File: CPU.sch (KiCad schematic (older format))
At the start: 14 parts, among them J8 SWD, U4 STM32F405RGTx, Y1 8MHz

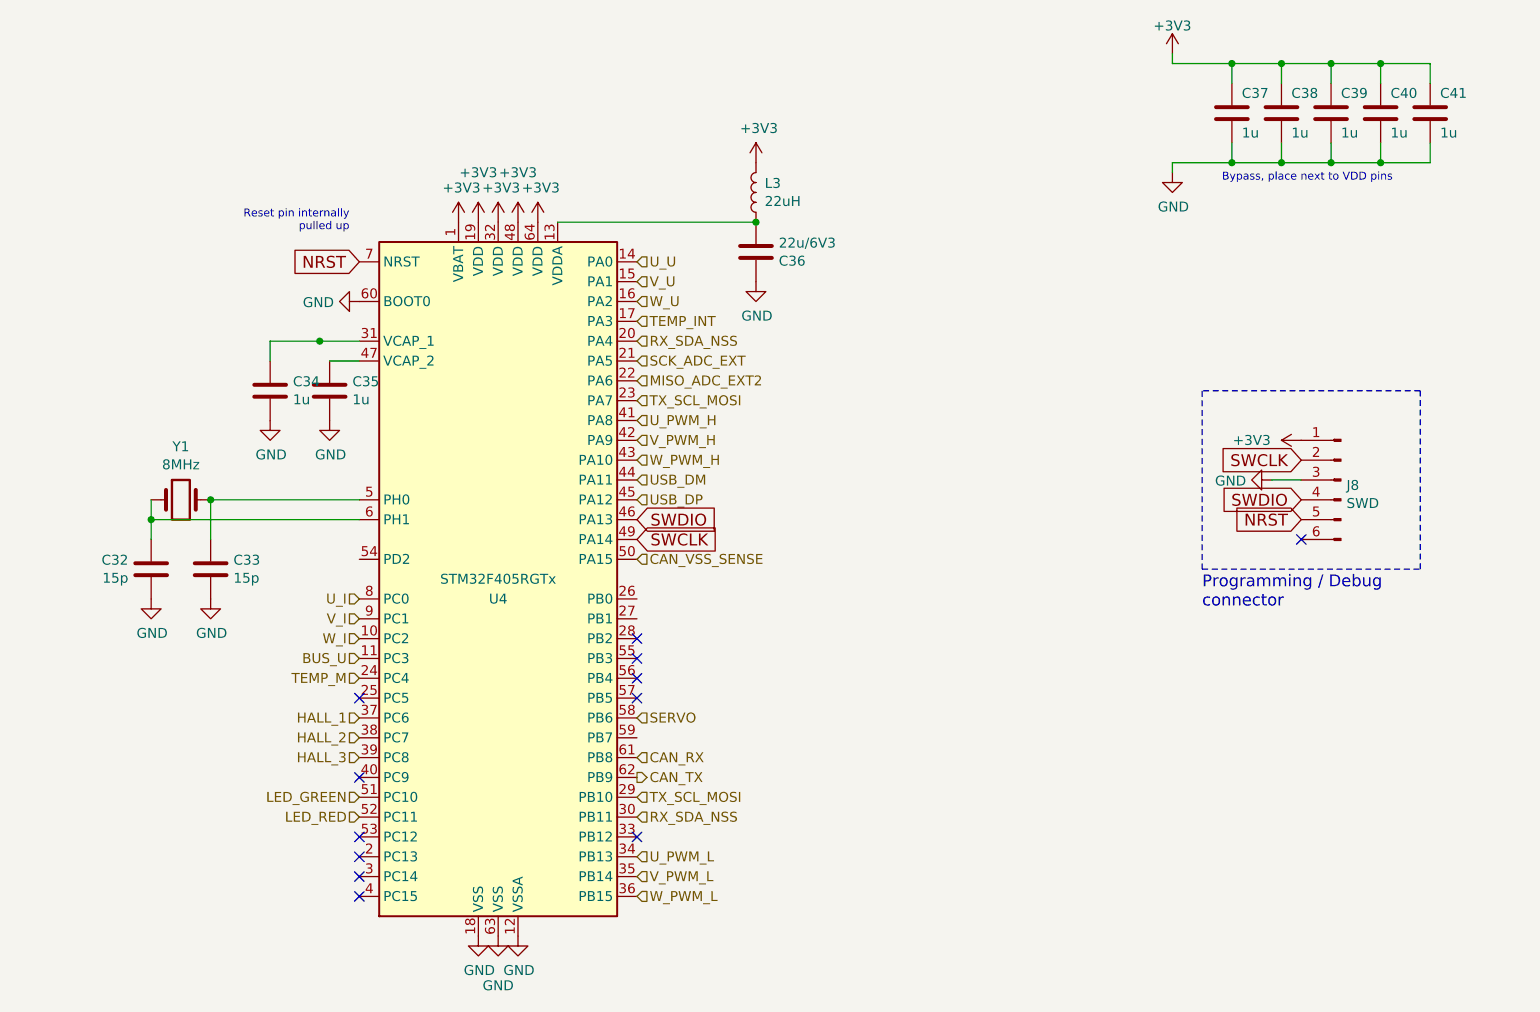
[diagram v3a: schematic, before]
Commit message: - reworked IO section -> now fully isolated - added fan output - sensor IO is now differential - exposed differential UART interface - fan pin not defined yet!
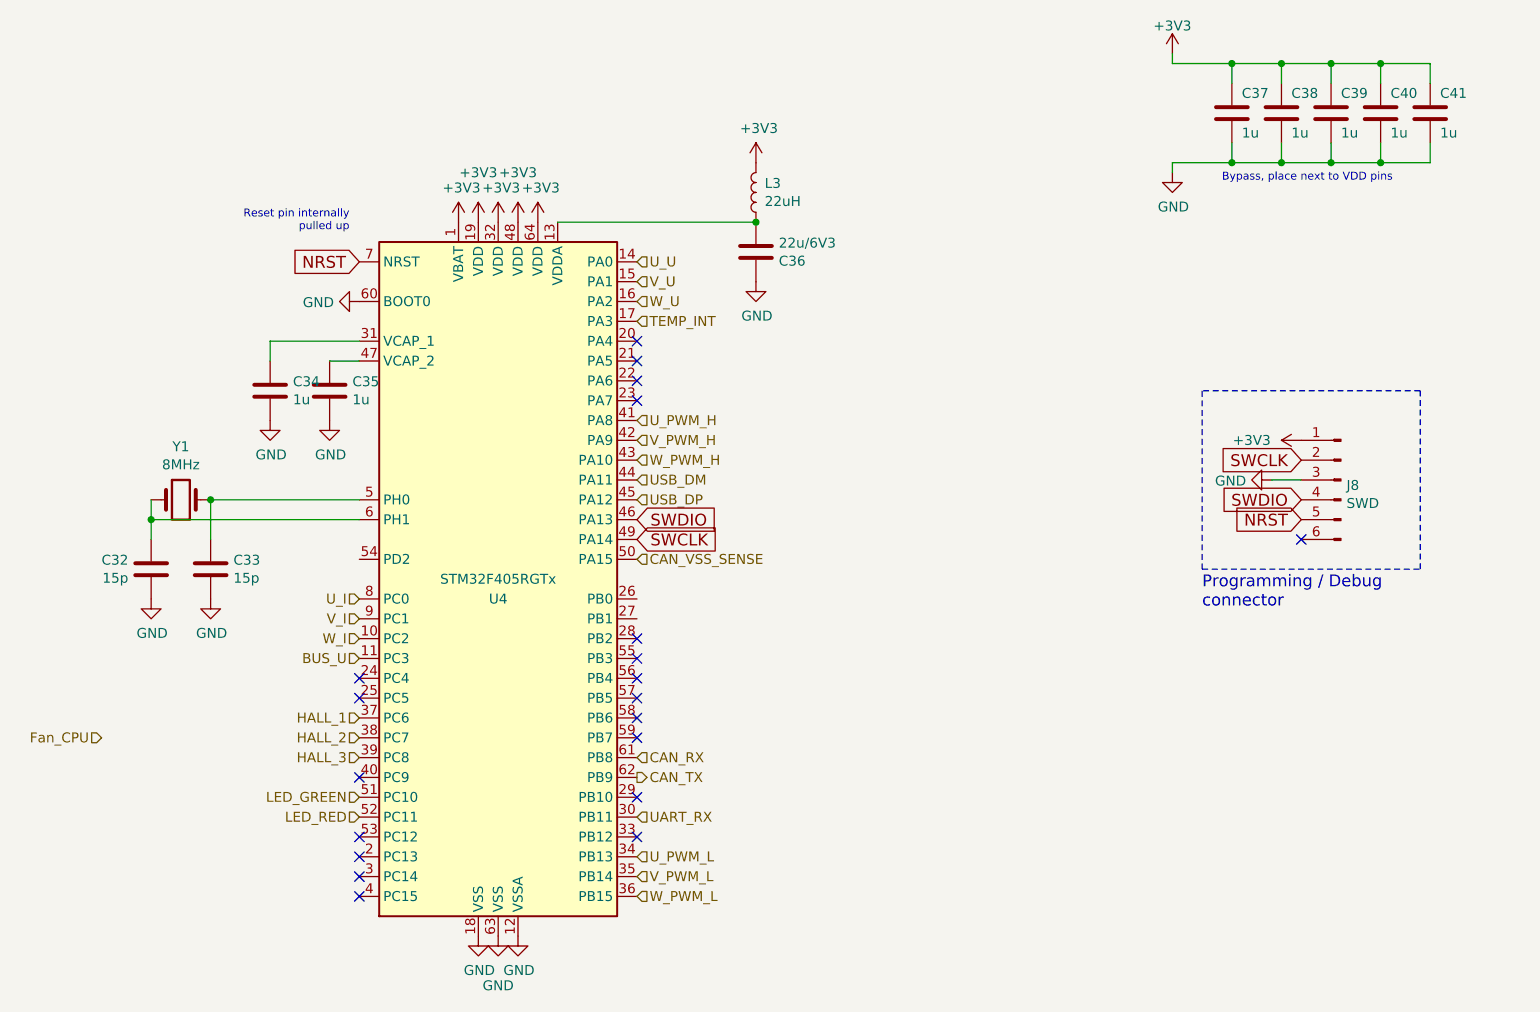
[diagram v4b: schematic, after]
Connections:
- net MISO_ADC_EXT2: no longer names the net of U4.22 (PA6)
- net RX_SDA_NSS: no longer names the net of U4.20 (PA4)
- net RX_SDA_NSS: no longer U4.30 (PB11)
- net SCK_ADC_EXT: no longer names the net of U4.21 (PA5)
- net SERVO: no longer names the net of U4.58 (PB6)
- net TEMP_M: no longer names the net of U4.24 (PC4)
- net TX_SCL_MOSI: no longer names the net of U4.23 (PA7)
- net TX_SCL_MOSI: no longer U4.29 (PB10)
- new net UART_RX: U4.30 (PB11)
- no-connect marks 12 -> 20
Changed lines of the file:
@@
 EESchema Schematic File Version 4
+LIBS:HSWR-cache
 EELAYER 30 0
 EELAYER END
@@
 Text HLabel 6400 2200 2    50   Input ~ 0
 W_U
-Text HLabel 6400 2300 2    50   Input ~ 0
-TEMP_INT
-Text HLabel 6400 2400 2    50   Input ~ 0
-RX_SDA_NSS
-Text HLabel 6400 2500 2    50   Input ~ 0
-SCK_ADC_EXT
-Text HLabel 6400 2600 2    50   Input ~ 0
-MISO_ADC_EXT2
-Text HLabel 6400 2700 2    50   Input ~ 0
-TX_SCL_MOSI
 Text HLabel 6400 2800 2    50   Input ~ 0
 U_PWM_H
@@
 Text HLabel 5000 4800 0    50   Input ~ 0
 LED_RED
-Text HLabel 6400 4300 2    50   Input ~ 0
-SERVO
 Text HLabel 6400 4500 2    50   Input ~ 0
 CAN_RX
 Text HLabel 6400 4600 2    50   Output ~ 0
 CAN_TX
-Text HLabel 6400 4700 2    50   Input ~ 0
-TX_SCL_MOSI
-Text HLabel 6400 4800 2    50   Input ~ 0
-RX_SDA_NSS
 Text HLabel 6400 5000 2    50   Input ~ 0
 U_PWM_L
@@
 Text HLabel 5000 4000 0    50   Input ~ 0
 BUS_U
-Text HLabel 5000 4100 0    50   Input ~ 0
-TEMP_M
 Text HLabel 5000 4300 0    50   Input ~ 0
 HALL_1
@@
 	5000 2500 4850 2500
 Wire Wire Line
-	5000 2400 4800 2400
-Wire Wire Line
 	4550 2400 4550 2500
 $Comp
@@
 $EndComp
 Connection ~ 4250 3200
-Connection ~ 4800 2400
-Wire Wire Line
-	4800 2400 4550 2400
 Connection ~ 7000 1800
+Wire Wire Line
+	4550 2400 5000 2400
+Text HLabel 3700 4400 0    50   Input ~ 0
+Fan_CPU
+NoConn ~ 6400 4700
+NoConn ~ 6400 4300
+NoConn ~ 6400 4400
+NoConn ~ 6400 2500
+NoConn ~ 6400 2600
+NoConn ~ 6400 2700
+Text HLabel 6400 4800 2    50   Input ~ 0
+UART_RX
+Text HLabel 6400 2300 2    50   Input ~ 0
+TEMP_INT
+NoConn ~ 6400 2400
+NoConn ~ 5000 4100
 $EndSCHEMATC

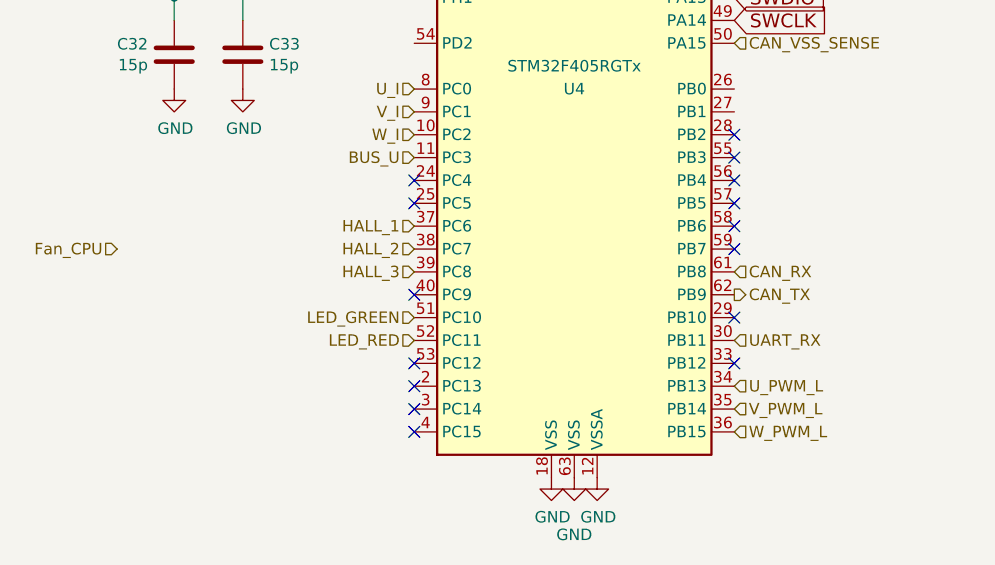
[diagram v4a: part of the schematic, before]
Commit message: - added high power capabilities to fan output - moved CAN isolator - connected fan output to PB10 (TIM2_CH3)
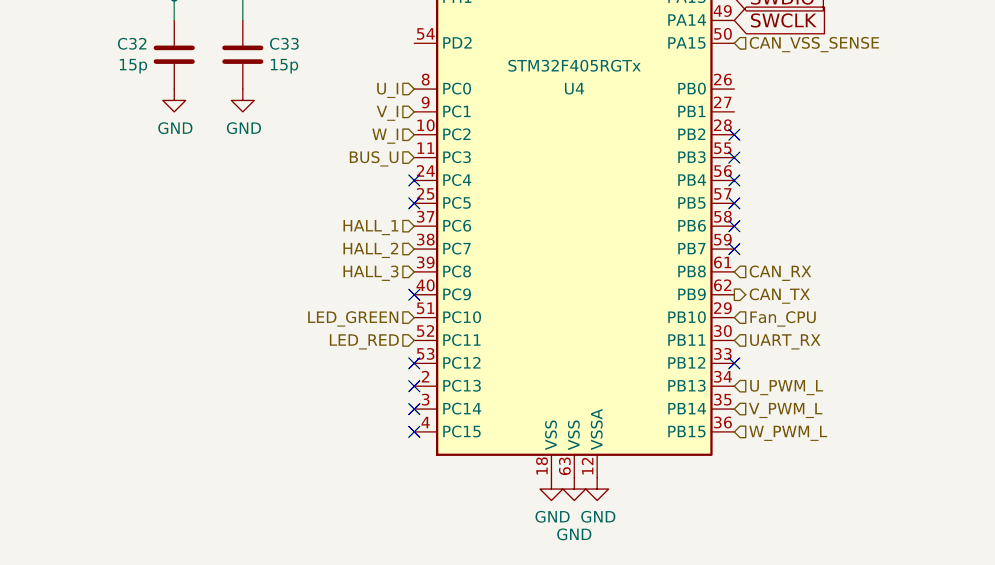
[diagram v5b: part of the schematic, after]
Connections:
- net Fan_CPU: now also U4.29 (PB10)
- no-connect marks 20 -> 19
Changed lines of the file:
@@
 EESchema Schematic File Version 4
-LIBS:HSWR-cache
 EELAYER 30 0
 EELAYER END
@@
 Wire Wire Line
 	4550 2400 5000 2400
-Text HLabel 3700 4400 0    50   Input ~ 0
+Text HLabel 6400 4700 2    50   Input ~ 0
 Fan_CPU
-NoConn ~ 6400 4700
 NoConn ~ 6400 4300
 NoConn ~ 6400 4400

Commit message: - fixed ISP connector being mirrored - changed some footprints to get them 3D Models - added a preliminary BOM
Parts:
- Y1: footprint Crystal:Crystal_HC49-U_Vertical -> Crystal:Crystal_HC49-4H_Vertical
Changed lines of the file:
@@
 F 0 "Y1" H 4100 3468 50  0000 C CNN
 F 1 "8MHz" H 4100 3377 50  0000 C CNN
-F 2 "Crystal:Crystal_HC49-U_Vertical" H 4100 3200 50  0001 C CNN
+F 2 "Crystal:Crystal_HC49-4H_Vertical" H 4100 3200 50  0001 C CNN
 F 3 "~" H 4100 3200 50  0001 C CNN
 	1    4100 3200
